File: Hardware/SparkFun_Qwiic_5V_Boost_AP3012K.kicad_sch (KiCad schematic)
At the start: 34 parts, among them J1 Qwiic_RA, J2 Qwiic_RA, J3 Conn_01x06, Q1 BSS138, Q2 BSS138, U1 AP3012

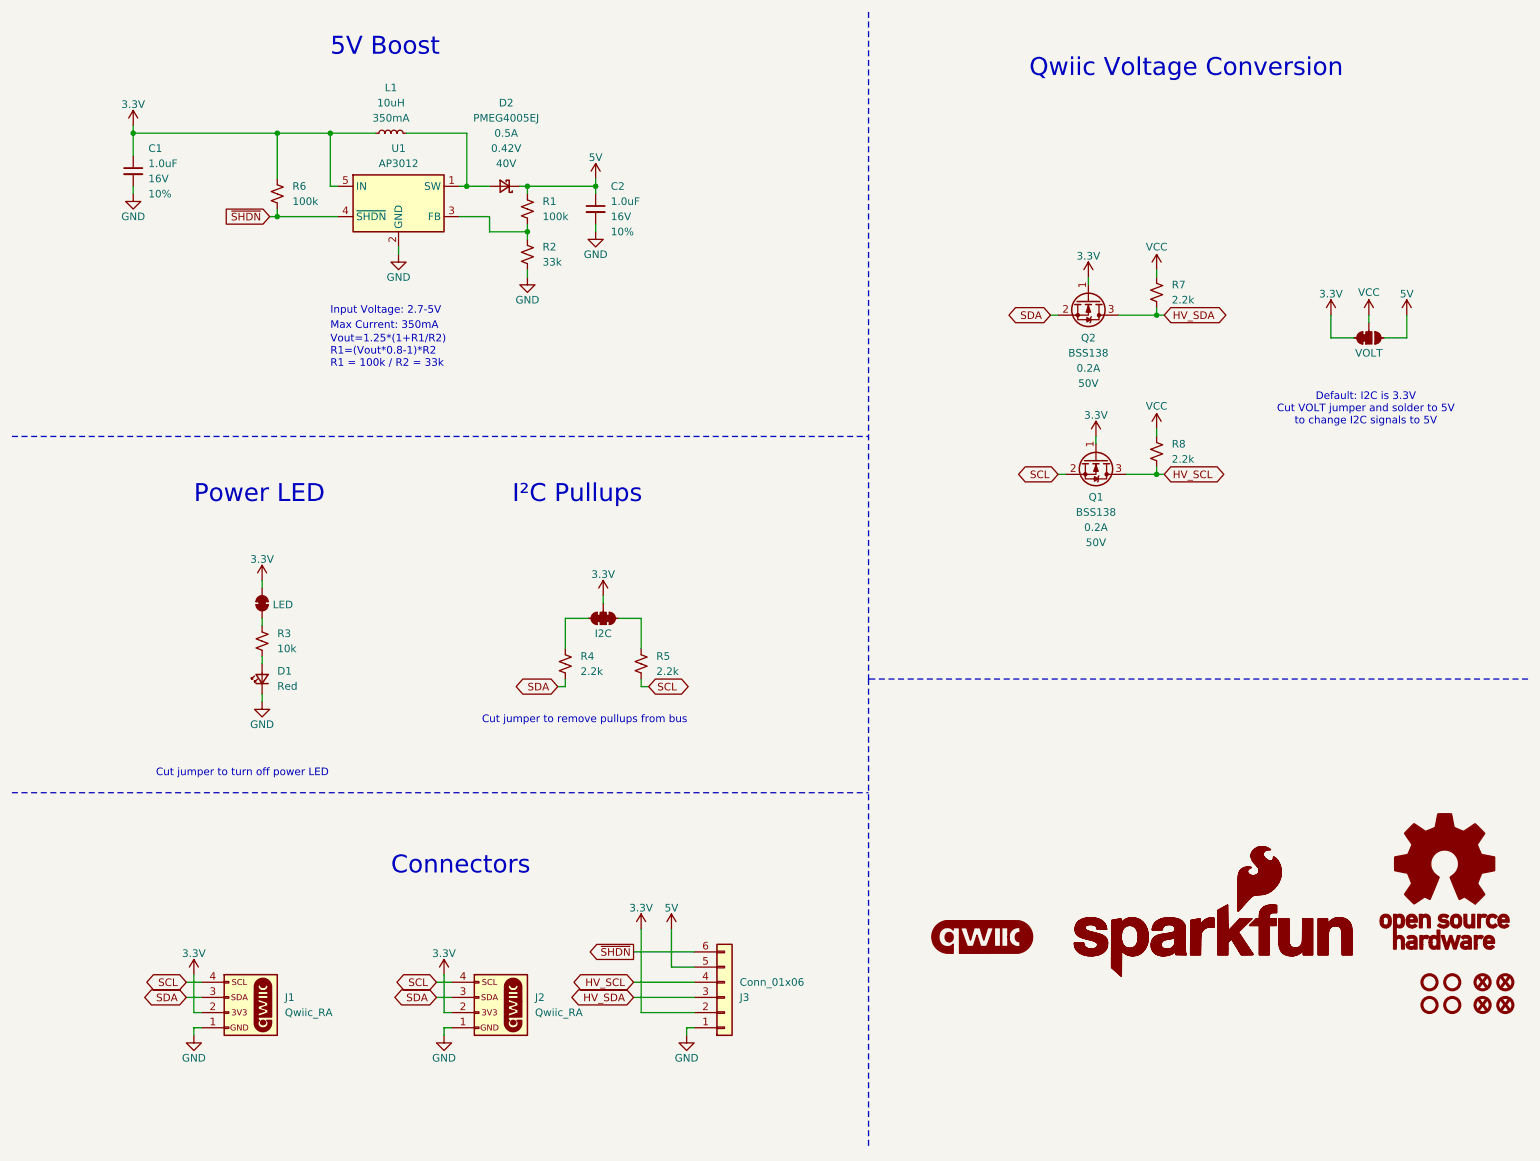
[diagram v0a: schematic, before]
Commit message: checklist run eng
-sch cleanup
-changed red led bias resistor to 4.7k
-adjusted thermal reliefs/spokes on power PTH headers (GND, 3V3, 5V)
-wire stubs removed
-dimensions added
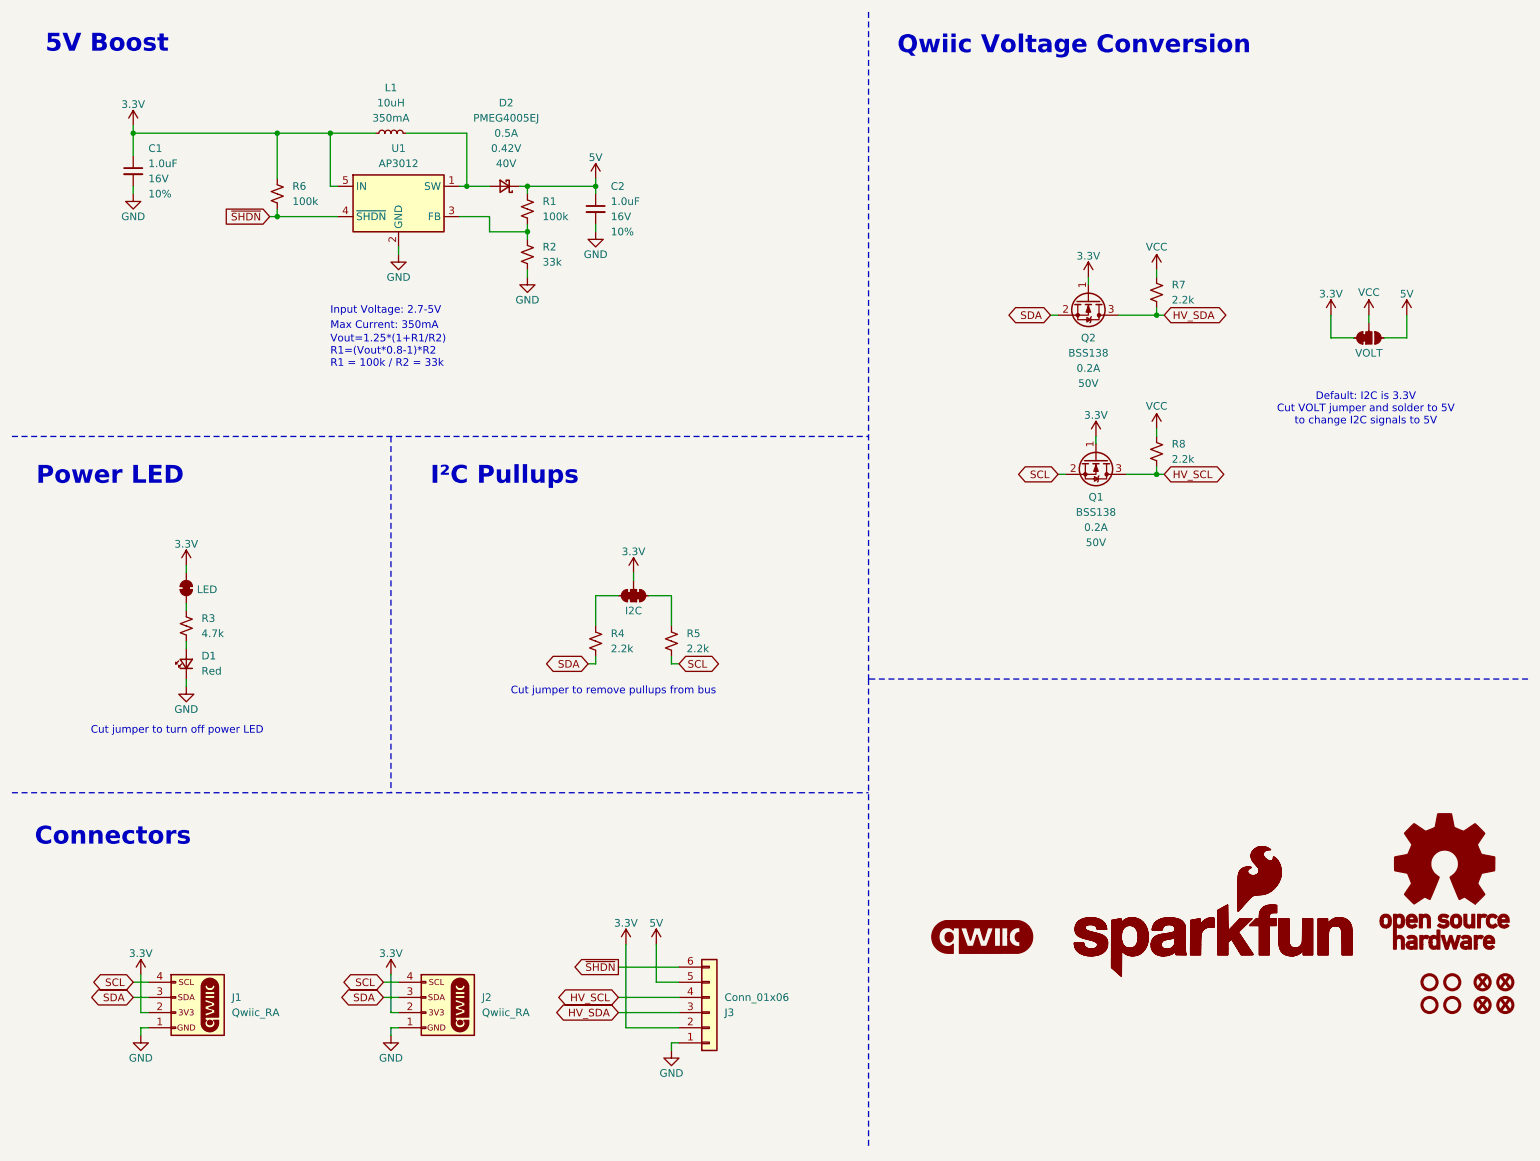
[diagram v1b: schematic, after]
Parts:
- removed R3: 10k, SparkFun-Resistor:R_0603_1608Metric, symbol SparkFun-Resistor:10k_0603
- added R3: 4.7k, SparkFun-Resistor:R_0603_1608Metric, symbol SparkFun-Resistor:4.7k_0603
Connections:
- net at D1.2 (A): now also R3.1
- net at JP1.1 (A): now also R3.2
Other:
- moved on the sheet: D1, J1, J2, J3, R4, R5

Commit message: design review changes part 1
-changed silk for logic jumper to PTH LOGIC LEVEL
-Added dashed lines around ADS/SCL PHT headers to show these logic levels are set by LOGIC jumper.
-Changed Value of JP3 to LOGIC
-un-bolded sch block title texts, switched to blue color
-aligned PWR silk label with LED perfectly
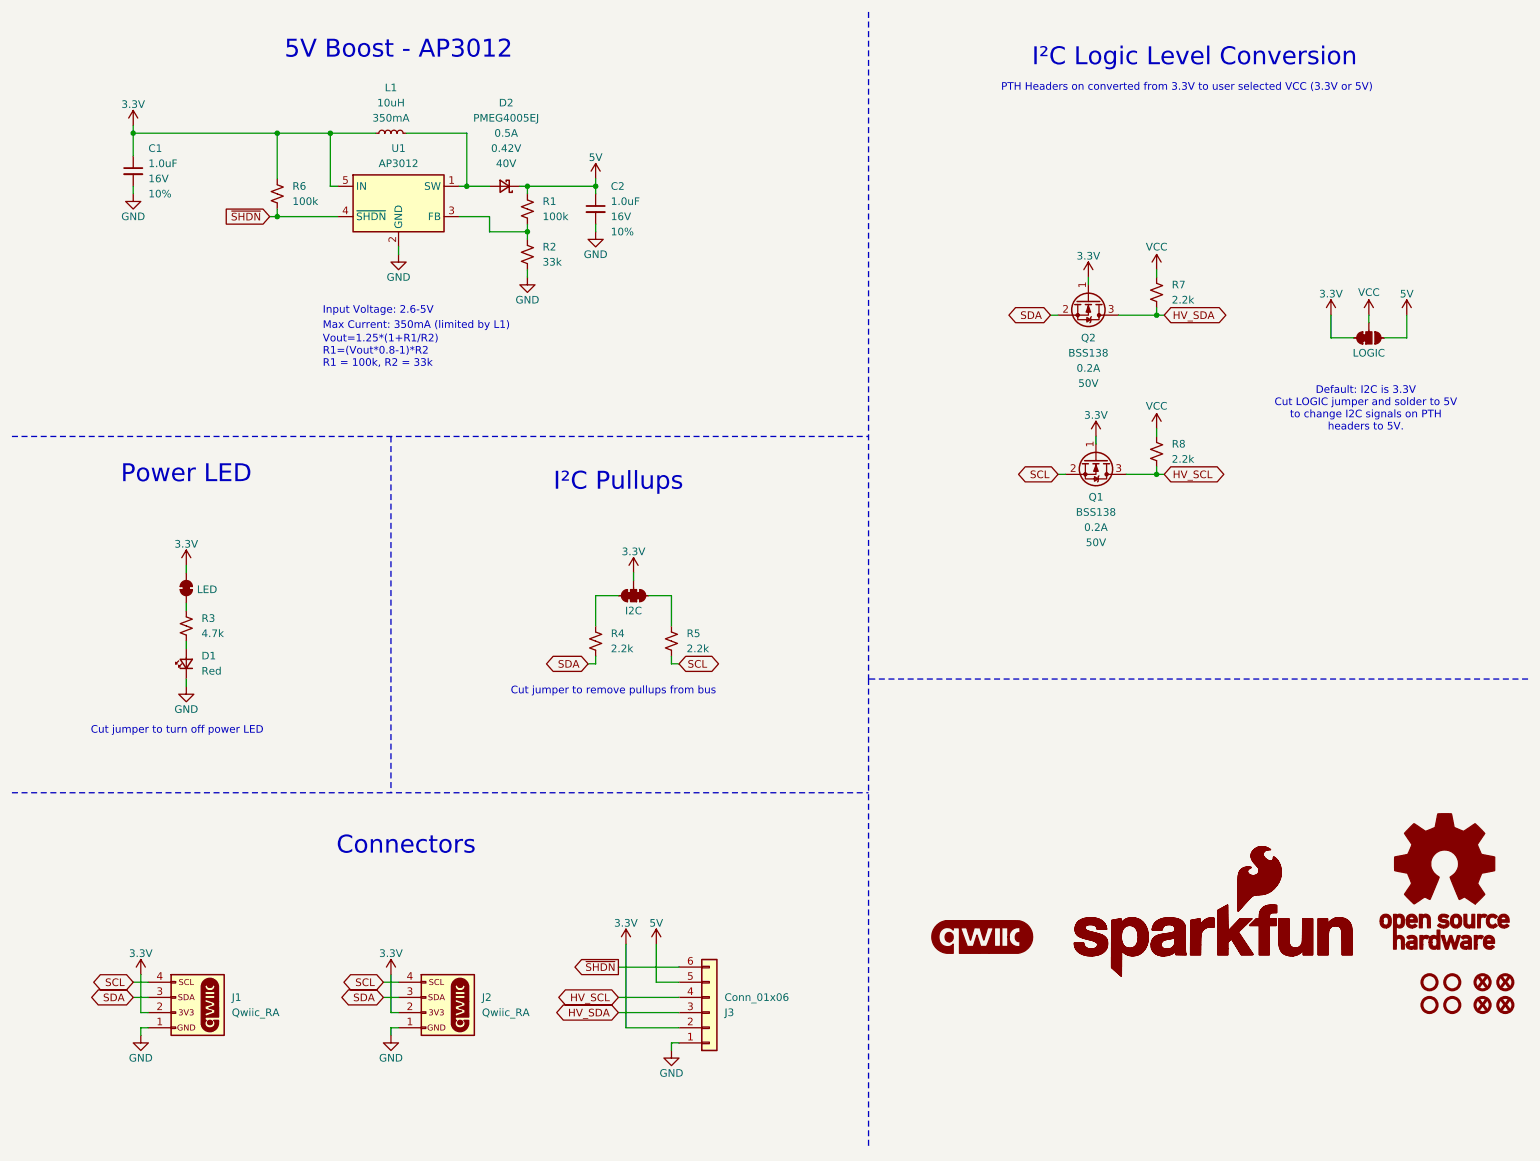
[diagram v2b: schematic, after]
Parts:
- JP3: value VOLT -> LOGIC
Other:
- note added: "5V Boost - AP3012"
- note added: "Default: I2C is 3.3V Cut LOGIC jumper and solder to 5V to change I2C signals on PTH headers to 5V."
- note added: "Input Voltage: 2.6-5V"
- note added: "I²C Logic Level Conversion"
- note added: "Max Current: 350mA (limited by L1)"
- note added: "PTH Headers on converted from 3.3V to user selected VCC (3.3V or 5V)"
- note added: "Vout=1.25*(1+R1/R2) R1=(Vout*0.8-1)*R2 R1 = 100k, R2 = 33k"
- note removed: "5V Boost"
- note removed: "Default: I2C is 3.3V Cut VOLT jumper and solder to 5V to change I2C signals to 5V"
- note removed: "Input Voltage: 2.7-5V"
- note removed: "Max Current: 350mA"
- note removed: "Qwiic Voltage Conversion"
- note removed: "Vout=1.25*(1+R1/R2) R1=(Vout*0.8-1)*R2 R1 = 100k / R2 = 33k"
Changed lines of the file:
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@@
 		(date "2025-02-10")
 		(rev "v10")
-		(comment 1 "Based off the Indoor Air Quality Combo by N. Seidle")
-		(comment 2 "Designed by: P. Lewis")
+		(comment 1 "SparkX Qwiic Boost by N. Seidle")
+		(comment 2 "Based off the Indoor Air Quality Combo and the")
+		(comment 3 "Designed by: P. Lewis")
 	)
 	(junction
@@
 		)
 	)
-	(text "I²C Pullups"
+	(text "PTH Headers on converted from 3.3V to user selected VCC (3.3V or 5V)"
 		(exclude_from_sim no)
-		(at 82.804 92.202 0)
-		(effects
-			(font
-				(size 3 3)
-				(thickness 0.6)
-				(bold yes)
-				(color 132 0 0 1)
+		(at 209.55 25.4 0)
+		(effects
+			(font
+				(size 1.27 1.27)
+				(color 132 132 132 1)
+			)
+		)
+	)
+	(text "Input Voltage: 2.6-5V"
+		(exclude_from_sim no)
+		(at 64.77 63.5 0)
+		(effects
+			(font
+				(size 1.27 1.27)
+				(color 132 132 132 1)
 			)
 			(justify left bottom)
 		)
 	)
-	(text "Power LED"
+	(text "Vout=1.25*(1+R1/R2)\nR1=(Vout*0.8-1)*R2\nR1 = 100k, R2 = 33k"
 		(exclude_from_sim no)
-		(at 16.764 92.202 0)
-		(effects
-			(font
-				(size 3 3)
-				(thickness 0.6)
-				(bold yes)
-				(color 132 0 0 1)
+		(at 64.77 72.39 0)
+		(effects
+			(font
+				(size 1.27 1.27)
+				(color 132 132 132 1)
 			)
 			(justify left bottom)
 		)
 	)
-	(text "Input Voltage: 2.7-5V"
-		(exclude_from_sim no)
-		(at 66.04 63.5 0)
-		(effects
-			(font
-				(size 1.27 1.27)
-				(color 132 132 132 1)
-			)
-			(justify left bottom)
-		)
-	)
-	(text "Connectors"
-		(exclude_from_sim no)
-		(at 16.51 152.654 0)
-		(effects
-			(font
-				(size 3 3)
-				(thickness 0.6)
-				(bold yes)
-				(color 132 0 0 1)
-			)
-			(justify left bottom)
-		)
-	)
-	(text "Vout=1.25*(1+R1/R2)\nR1=(Vout*0.8-1)*R2\nR1 = 100k / R2 = 33k"
-		(exclude_from_sim no)
-		(at 66.04 72.39 0)
-		(effects
-			(font
-				(size 1.27 1.27)
-				(color 132 132 132 1)
-			)
-			(justify left bottom)
-		)
-	)
-	(text "Default: I2C is 3.3V\nCut VOLT jumper and solder to 5V\nto change I2C signals to 5V"
+	(text "Default: I2C is 3.3V\nCut LOGIC jumper and solder to 5V\nto change I2C signals on PTH \nheaders to 5V."
 		(exclude_from_sim no)
 		(at 239.522 79.248 0)
@@
 				(color 132 132 132 1)
 			)
-		)
-	)
-	(text "Qwiic Voltage Conversion"
-		(exclude_from_sim no)
-		(at 161.036 20.066 0)
-		(effects
-			(font
-				(size 3 3)
-				(thickness 0.6)
-				(bold yes)
-				(color 132 0 0 1)
-			)
-			(justify left bottom)
 		)
 	)
@@
 		)
 	)
-	(text "5V Boost"
+	(text "I²C Logic Level Conversion"
 		(exclude_from_sim no)
-		(at 18.288 19.812 0)
+		(at 210.82 20.32 0)
 		(effects
 			(font
 				(size 3 3)
-				(thickness 0.6)
-				(bold yes)
-				(color 132 0 0 1)
-			)
-			(justify left bottom)
-		)
-	)
-	(text "Max Current: 350mA"
+			)
+		)
+	)
+	(text "Max Current: 350mA (limited by L1)"
 		(exclude_from_sim no)
-		(at 66.04 66.04 0)
+		(at 64.77 66.04 0)
 		(effects
 			(font
@@
 			)
 			(justify left bottom)
+		)
+	)
+	(text "Power LED"
+		(exclude_from_sim no)
+		(at 41.91 90.17 0)
+		(effects
+			(font
+				(size 3 3)
+			)
+		)
+	)
+	(text "Connectors"
+		(exclude_from_sim no)
+		(at 78.74 152.4 0)
+		(effects
+			(font
+				(size 3 3)
+			)
+		)
+	)
+	(text "I²C Pullups"
+		(exclude_from_sim no)
+		(at 114.3 91.44 0)
+		(effects
+			(font
+				(size 3 3)
+			)
+		)
+	)
+	(text "5V Boost - AP3012"
+		(exclude_from_sim no)
+		(at 77.47 19.05 0)
+		(effects
+			(font
+				(size 3 3)
+			)
 		)
 	)
@@
 			)
 		)
-		(property "Value" "VOLT"
+		(property "Value" "LOGIC"
 			(at 240.03 69.85 0)
 			(effects
